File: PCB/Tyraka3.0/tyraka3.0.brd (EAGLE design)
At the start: 60 x 170 mm, 45 parts, among them Q1 IRF8313P, Q2 IRF8313P, T1 BC846, T2 BC846, U2 GY-521MPU6050

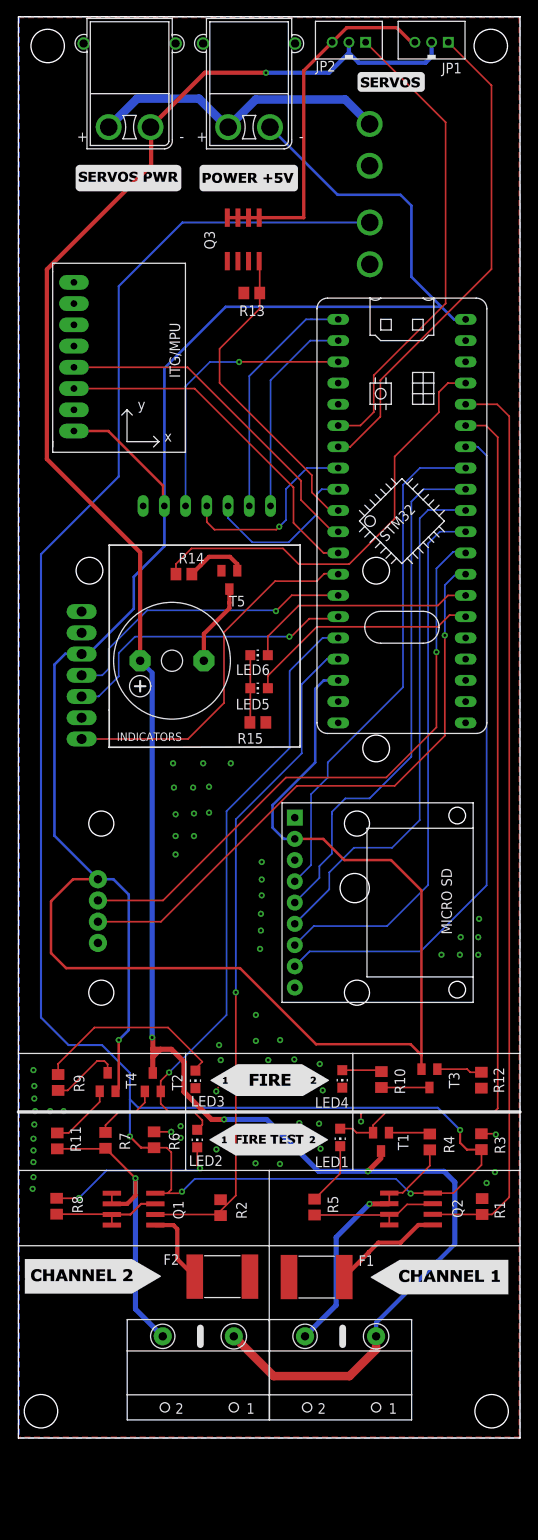
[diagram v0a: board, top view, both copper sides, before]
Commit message: add_few_features
add_few_features to board like round corners and place for jlc signature
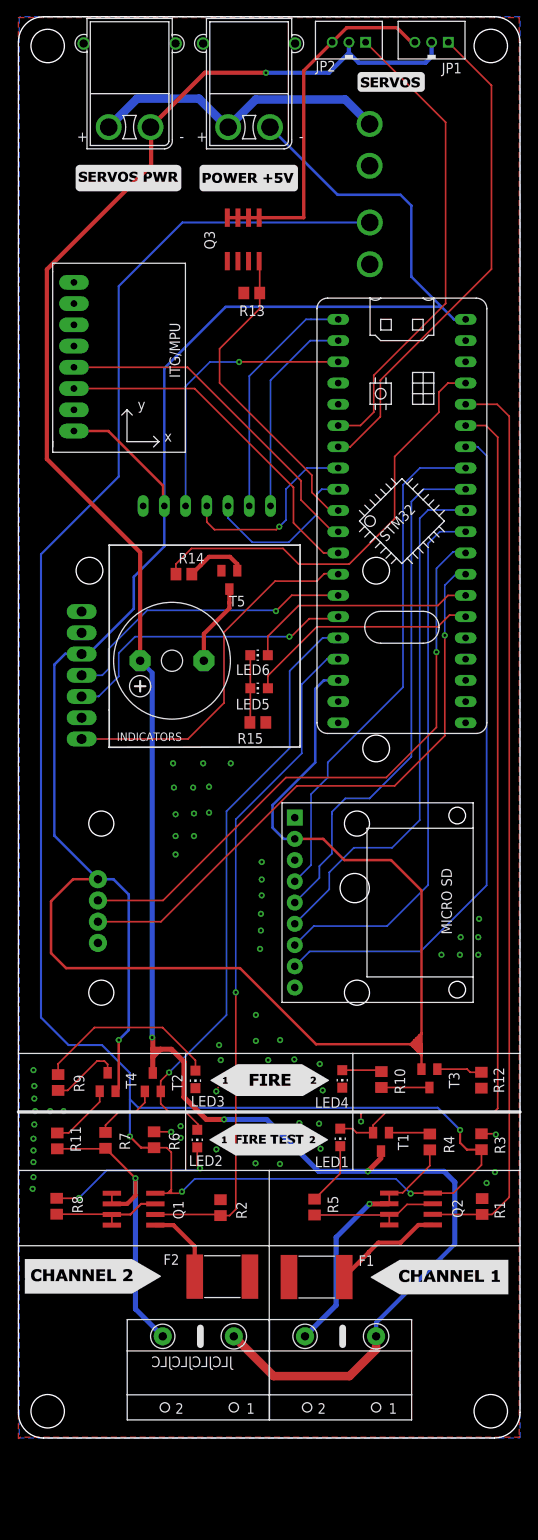
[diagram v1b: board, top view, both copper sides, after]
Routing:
- net +5V: track 315.4 -> 323.0 mm
- net N$17: track 23.4 -> 22.4 mm
- net FIRE_CHANNEL_2_TEST: track 72.8 -> 71.8 mm
- net FIRE_CHANNEL_ARMING: track 245.4 -> 246.2 mm
- net FIRE_CHANNEL_2_EN: track 81.0 -> 81.7 mm
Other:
- outline, holes or cut-outs redrawn
- board text added: "JLCJLCJLCJLC"

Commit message: swap 5 with 3v3
add
-3v3 swap with 5
-add dzielniknapiecia
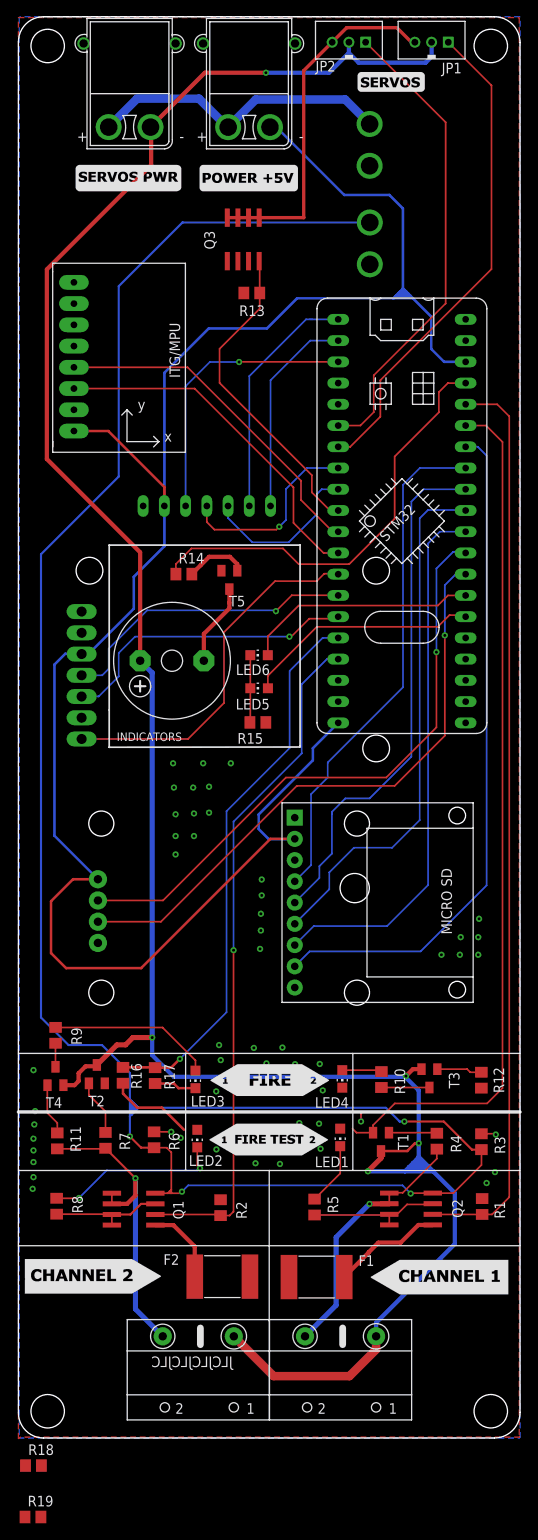
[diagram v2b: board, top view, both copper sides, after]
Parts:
- added R16, R17, R18, R19: 1k, rcl:R0805
- moved T2 6.76 mm to (9.38, 43.5)
- moved T4 6.28 mm to (4.43, 43.3)
- moved R9 5.65 mm to (4.45, 48.2)
- moved R4 0.84 mm to (50.0, 35.5)
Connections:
- removed net +5V: SD1.P2, T3.E, T4.E, U$1.3, U$2.VCC, U$3.5V, U$3.5V1, U$4.VCC, U$6.P$2, U2.VCC
- new net +3V3: SD1.P2, U$1.3, U$2.VCC, U$3.3.3V1, U$3.3V3, U$4.VCC, U$6.P$2, U2.VCC
- new net 5V1: U$3.5V1
- new net N$15: LED2.A, R16.1, T2.2
- new net N$20: LED1.A, R18.1, T1.2
- net FIRE_CHANNEL_1_TEST: now also R18.2, R19.2; no longer LED1.A, T1.2
- net FIRE_CHANNEL_2_TEST: now also R16.2, R17.1; no longer LED2.A, T2.2
- net GND: now also R17.2, R19.1
- net V+: now also T3.E, T4.E
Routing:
- net +5V: track 323.0 -> 0.00 mm, vias 1 -> 0
- net +3V3: track 0.00 -> 238.9 mm
- net V+: track 260.4 -> 291.7 mm, vias 4 -> 5
- net N$15: track 0.00 -> 10.3 mm
- net N$16: track 8.56 -> 2.82 mm
- net FIRE_CHANNEL_2_TEST: track 71.8 -> 66.5 mm
- net GND: track 4.83 -> 10.0 mm, vias 59 -> 52
- net FIRE_CHANNEL_ARMING: track 246.2 -> 250.7 mm
- net N$17: track 22.4 -> 19.6 mm
- net FIRE_CHANNEL_1_TEST: track 105.5 -> 103.4 mm
- net N$18: track 7.89 -> 6.22 mm
- net N$10: track 8.03 -> 6.69 mm
- net N$9: track 4.95 -> 5.75 mm

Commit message: dzielnik napiecia
add dzielnik napiecia
and few fixes
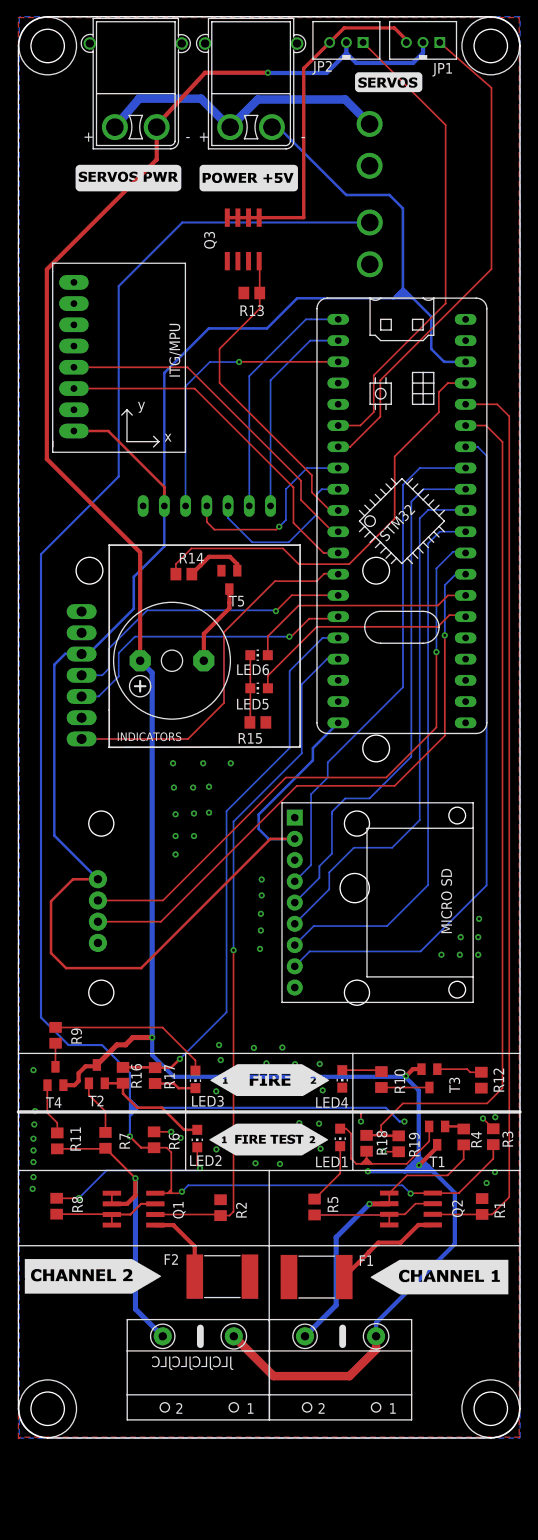
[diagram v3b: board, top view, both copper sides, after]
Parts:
- moved R19 62.5 mm to (45.5, 35.2), turned to 90 degrees
- moved R18 55.4 mm to (41.6, 35.2), turned to 90 degrees
- moved T1 6.76 mm to (50.1, 36.2)
- moved R4 3.25 mm to (53.3, 36.0)
- moved R3 1.53 mm to (56.8, 36.0)
- moved JP1 1.02 mm to (48.4, 166.9)
- moved U$5 0.74 mm to (11.5, 156.8)
- moved JP2 0.30 mm to (39.2, 166.9)
- moved U$6 0.24 mm to (25.3, 156.8)
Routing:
- net N$20: track 0.00 -> 22.5 mm
- net FIRE_CHANNEL_ARMING: track 250.7 -> 241.7 mm
- net V+: track 291.7 -> 286.9 mm
- net FIRE_CHANNEL_1_TEST: track 103.4 -> 107.7 mm
- net N$15: track 10.3 -> 14.1 mm
- net CHANNEL_1: track 31.2 -> 35.0 mm
- net N$9: track 5.75 -> 2.64 mm
- net GND: track 10.0 -> 11.9 mm, vias 52 -> 54
- net N$3: track 16.0 -> 17.0 mm
- net SERVO_2: track 59.0 -> 59.6 mm
- net SCREW_SWITCH_GND: track 36.6 -> 36.0 mm
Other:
- outline, holes or cut-outs redrawn
